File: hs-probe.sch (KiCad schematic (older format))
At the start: 57 parts, among them J1 USB_C_Receptacle_USB2.0, J2 Castellated Vias, J3 Castellated Vias, J4 Castellated Vias, J5 tag-connect-swd, Q101 DMP2110UW-7, U1 hs-probe-stm32, U2 12 MHz, U3 MIC5353, U4 NUF8401MNT4G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

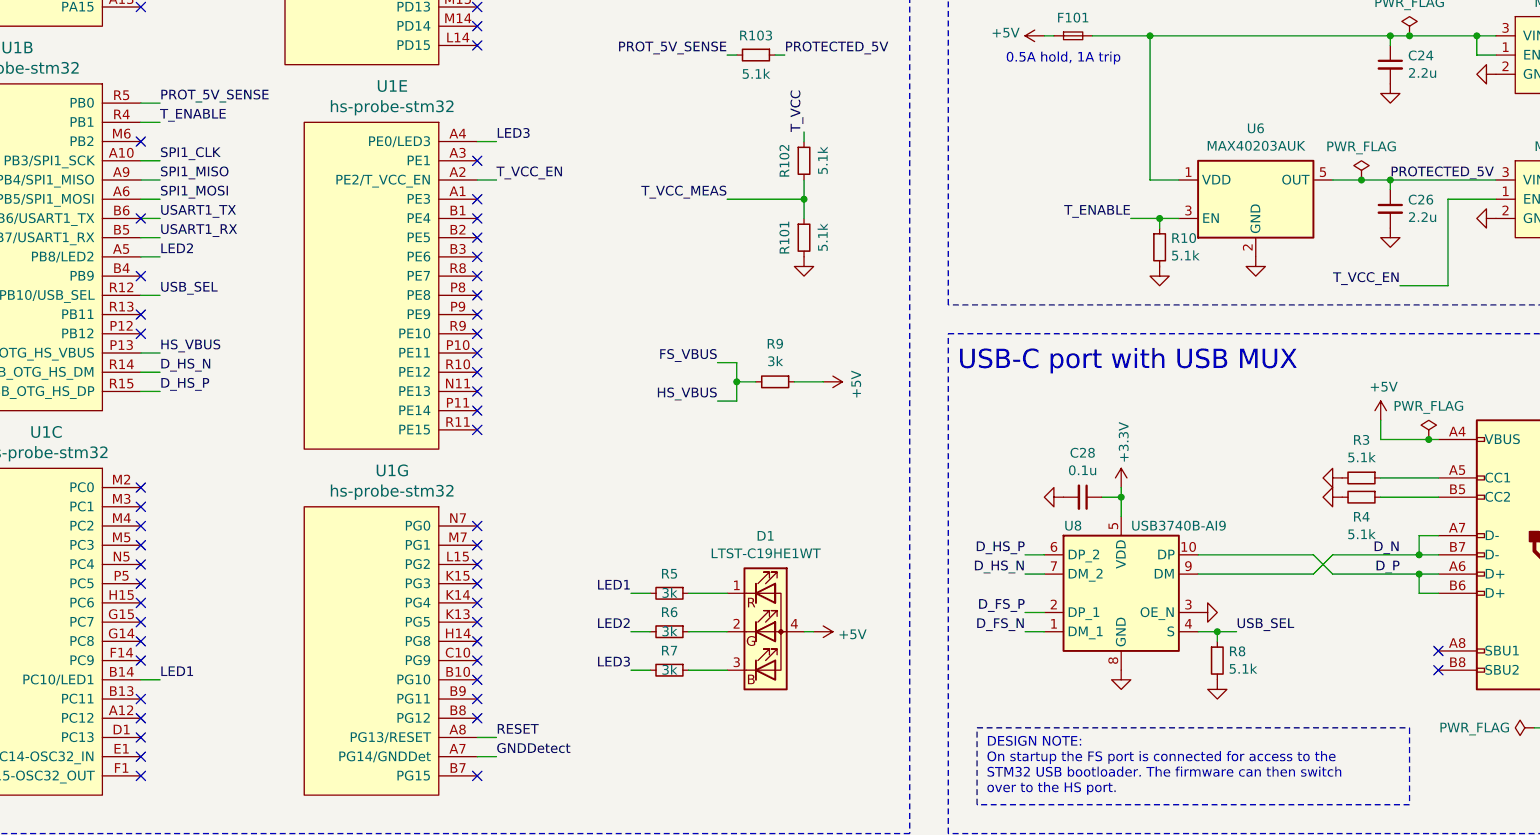
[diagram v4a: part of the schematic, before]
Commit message: v1.4, now without the USB mux
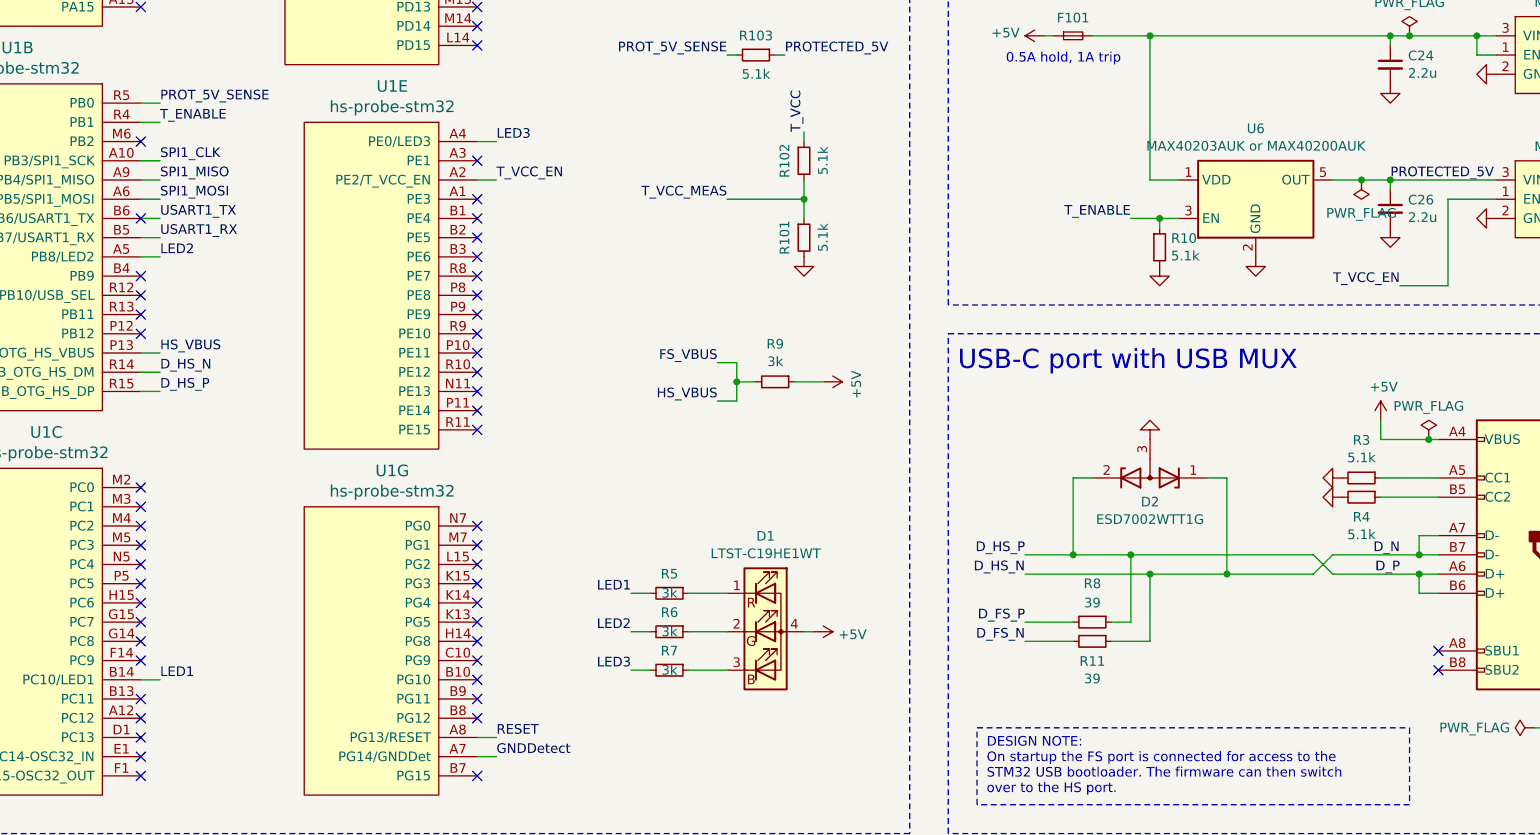
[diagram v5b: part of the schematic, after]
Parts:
- removed C28: 0.1u, passive:C_0402, symbol Device:C_Small
- removed U8: USB3740B-AI9, Package_DFN_QFN:UQFN-10_1.6x2.1mm_P0.5mm, symbol Interface_USB:USB3740B-AI9
- added D2: ESD7002WTT1G, sot:SOT-323, symbol Device:D_Zener_x2_ACom_KKA
- added R11: 39, passive:R_0402, symbol Device:R_Small
- R8: value 5.1k -> 39
- U6: value MAX40203AUK -> MAX40203AUK or MAX40200AUK
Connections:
- net D_N is gone; now on net D_HS_N: J1.A7 (D-), J1.B7 (D-)
- net D_P is gone; now on net D_HS_P: J1.A6 (D+), J1.B6 (D+)
- net D_FS_N: now also R11.2
- net D_FS_P: now also R8.2
- net D_HS_N: now also D2.1 (K), R11.1
- net D_HS_P: now also R8.1, D2.2 (K)
- net GND: now also D2.3 (A); no longer R8.2
- net USB_SEL: no longer names the net of U1.R12 (PB10/USB_SEL)
- net USB_SEL: no longer R8.1
- no-connect marks 84 -> 85
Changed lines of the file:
@@
 Sheet 1 1
 Title "Rusty High-Speed Probe"
-Date "2020-11-28"
-Rev "v1.3"
+Date "2021-05-21"
+Rev "v1.4"
 Comp ""
 Comment1 ""
@@
 	8650 7700 8650 7750
 $Comp
-L Device:C_Small C26
-U 1 1 5E935363
-P 8650 7850
-F 0 "C26" H 8742 7896 50  0000 L CNN
-F 1 "2.2u" H 8742 7805 50  0000 L CNN
-F 2 "passive:C_0402" H 8650 7850 50  0001 C CNN
-F 3 "~" H 8650 7850 50  0001 C CNN
-F 4 "10V, X5R" H 8650 7850 50  0001 C CNN "Tolerance"
-	1    8650 7850
-	1    0    0    -1
-$EndComp
-$Comp
 L Device:C_Small C24
 U 1 1 5E9D42F6
@@
 Text Label 6750 9650 2    50   ~ 0
 D_HS_P
-Wire Wire Line
-	6750 9650 6850 9650
-Wire Wire Line
-	6850 9750 6750 9750
-Text Label 6750 10050 2    50   ~ 0
+Text Label 6750 10100 2    50   ~ 0
 D_FS_N
-Text Label 6750 9950 2    50   ~ 0
+Text Label 6750 10000 2    50   ~ 0
 D_FS_P
-Wire Wire Line
-	6750 9950 6850 9950
-Wire Wire Line
-	6850 10050 6750 10050
-$Comp
-L power:GND #PWR0106
-U 1 1 5F27548A
-P 7250 10250
-F 0 "#PWR0106" H 7250 10000 50  0001 C CNN
-F 1 "GND" H 7255 10077 50  0001 C CNN
-F 2 "" H 7250 10250 50  0001 C CNN
-F 3 "" H 7250 10250 50  0001 C CNN
-	1    7250 10250
-	1    0    0    -1
-$EndComp
-$Comp
-L Device:C_Small C28
-U 1 1 5F275754
-P 7050 9350
-F 0 "C28" V 6821 9350 50  0000 C CNN
-F 1 "0.1u" V 6912 9350 50  0000 C CNN
-F 2 "passive:C_0402" H 7050 9350 50  0001 C CNN
-F 3 "~" H 7050 9350 50  0001 C CNN
-F 4 "25V, X7R" H 7050 9350 50  0001 C CNN "Tolerance"
-	1    7050 9350
-	0    1    1    0
-$EndComp
-$Comp
-L power:+3.3V #PWR0107
-U 1 1 5F276119
-P 7250 9300
-F 0 "#PWR0107" H 7250 9150 50  0001 C CNN
-F 1 "+3.3V" V 7265 9428 50  0000 L CNN
-F 2 "" H 7250 9300 50  0001 C CNN
-F 3 "" H 7250 9300 50  0001 C CNN
-	1    7250 9300
-	1    0    0    -1
-$EndComp
-Wire Wire Line
-	7150 9350 7250 9350
-Wire Wire Line
-	7250 9350 7250 9300
-Wire Wire Line
-	7250 9350 7250 9450
-Connection ~ 7250 9350
-$Comp
-L power:GND #PWR0108
-U 1 1 5F29B742
-P 6950 9350
-F 0 "#PWR0108" H 6950 9100 50  0001 C CNN
-F 1 "GND" H 6955 9177 50  0001 C CNN
-F 2 "" H 6950 9350 50  0001 C CNN
-F 3 "" H 6950 9350 50  0001 C CNN
-	1    6950 9350
-	0    1    1    0
-$EndComp
-$Comp
-L power:GND #PWR0109
-U 1 1 5F2BF882
-P 7650 9950
-F 0 "#PWR0109" H 7650 9700 50  0001 C CNN
-F 1 "GND" H 7655 9777 50  0001 C CNN
-F 2 "" H 7650 9950 50  0001 C CNN
-F 3 "" H 7650 9950 50  0001 C CNN
-	1    7650 9950
-	0    -1   -1   0
-$EndComp
-Wire Wire Line
-	7650 10050 7750 10050
-Text Label 7850 10050 0    50   ~ 0
-USB_SEL
-$Comp
-L Device:R_Small R8
-U 1 1 5F2D2B4D
-P 7750 10200
-F 0 "R8" H 7809 10246 50  0000 L CNN
-F 1 "5.1k" H 7809 10155 50  0000 L CNN
-F 2 "passive:R_0402" H 7750 10200 50  0001 C CNN
-F 3 "~" H 7750 10200 50  0001 C CNN
-F 4 "1%" H 7750 10200 50  0001 C CNN "Tolerance"
-	1    7750 10200
-	1    0    0    -1
-$EndComp
-$Comp
-L power:GND #PWR0110
-U 1 1 5F2D2B53
-P 7750 10300
-F 0 "#PWR0110" H 7750 10050 50  0001 C CNN
-F 1 "GND" H 7755 10127 50  0001 C CNN
-F 2 "" H 7750 10300 50  0001 C CNN
-F 3 "" H 7750 10300 50  0001 C CNN
-	1    7750 10300
-	1    0    0    -1
-$EndComp
-Wire Wire Line
-	7750 10100 7750 10050
-Connection ~ 7750 10050
-Wire Wire Line
-	7750 10050 7850 10050
-$Comp
-L Interface_USB:USB3740B-AI9 U8
-U 1 1 5F2F9B6C
-P 7250 9850
-F 0 "U8" H 7500 10200 50  0000 C CNN
-F 1 "USB3740B-AI9" H 6950 10200 50  0000 C CNN
-F 2 "Package_DFN_QFN:UQFN-10_1.6x2.1mm_P0.5mm" H 8450 9500 50  0001 C CNN
-F 3 "http://ww1.microchip.com/downloads/en/DeviceDoc/00001725D.pdf" H 7250 9750 50  0001 C CNN
-F 4 "USB3740B-AI9-TR" H 7250 9850 50  0001 C CNN "MPN"
-	1    7250 9850
-	-1   0    0    -1
-$EndComp
 $Comp
 L Connector:Conn_01x09_Female J2
@@
 	8350 9750 8800 9750
 Wire Wire Line
-	7650 9650 8250 9650
-Wire Wire Line
 	8350 9650 8250 9750
-Wire Wire Line
-	7650 9750 8250 9750
 Wire Wire Line
 	8350 9650 8800 9650
@@
 Wire Wire Line
 	2250 8100 2150 8100
-Wire Wire Line
-	2250 8300 2150 8300
-Text Label 2250 8300 0    50   ~ 0
-USB_SEL
 Text Label 2250 6700 0    50   ~ 0
 D_FS_P
@@
 P 7950 7800
 F 0 "U6" H 7950 8167 50  0000 C CNN
-F 1 "MAX40203AUK" H 7950 8076 50  0000 C CNN
+F 1 "MAX40203AUK or MAX40200AUK" H 7950 8076 50  0000 C CNN
 F 2 "sot:SOT-23-5" H 7950 8300 50  0001 C CNN
 F 3 "https://datasheets.maximintegrated.com/en/ds/MAX40203.pdf" H 7950 8300 50  0001 C CNN
@@
 F 3 "~" H 8500 7700 50  0001 C CNN
 	1    8500 7700
-	1    0    0    -1
+	-1   0    0    1
 $EndComp
 Connection ~ 8500 7700
@@
 Text Notes 6650 7100 0    50   ~ 0
 0.5A hold, 1A trip
+$Comp
+L Device:C_Small C26
+U 1 1 5E935363
+P 8650 7850
+F 0 "C26" H 8742 7896 50  0000 L CNN
+F 1 "2.2u" H 8742 7805 50  0000 L CNN
+F 2 "passive:C_0402" H 8650 7850 50  0001 C CNN
+F 3 "~" H 8650 7850 50  0001 C CNN
+F 4 "10V, X5R" H 8650 7850 50  0001 C CNN "Tolerance"
+	1    8650 7850
+	1    0    0    -1
+$EndComp
+Wire Wire Line
+	6750 9650 7000 9650
+Wire Wire Line
+	6750 9750 7400 9750
+$Comp
+L Device:R_Small R11
+U 1 1 60B173EB
+P 7100 10100
+F 0 "R11" V 7204 10100 50  0000 C CNN
+F 1 "39" V 7295 10100 50  0000 C CNN
+F 2 "passive:R_0402" H 7100 10100 50  0001 C CNN
+F 3 "~" H 7100 10100 50  0001 C CNN
+F 4 "1%" H 7100 10100 50  0001 C CNN "Tolerance"
+	1    7100 10100
+	0    1    1    0
+$EndComp
+$Comp
+L Device:R_Small R8
+U 1 1 60B17924
+P 7100 10000
+F 0 "R8" V 6900 10000 50  0000 C CNN
+F 1 "39" V 7000 10000 50  0000 C CNN
+F 2 "passive:R_0402" H 7100 10000 50  0001 C CNN
+F 3 "~" H 7100 10000 50  0001 C CNN
+F 4 "1%" H 7100 10000 50  0001 C CNN "Tolerance"
+	1    7100 10000
+	0    1    1    0
+$EndComp
+Wire Wire Line
+	6750 10000 7000 10000
+Wire Wire Line
+	6750 10100 7000 10100
+Wire Wire Line
+	7200 10000 7300 10000
+Wire Wire Line
+	7300 10000 7300 9650
+Connection ~ 7300 9650
+Wire Wire Line
+	7300 9650 8250 9650
+Wire Wire Line
+	7200 10100 7400 10100
+Wire Wire Line
+	7400 10100 7400 9750
+Connection ~ 7400 9750
+Wire Wire Line
+	7400 9750 7800 9750
+$Comp
+L Device:D_Zener_x2_ACom_KKA D2
+U 1 1 60B85F80
+P 7400 9250
+F 0 "D2" H 7400 9375 50  0000 C CNN
+F 1 "ESD7002WTT1G" H 7400 9466 50  0000 C CNN
+F 2 "sot:SOT-323" H 7400 9250 50  0001 C CNN
+F 3 "https://www.onsemi.com/pdf/datasheet/esd7002-d.pdf" H 7400 9250 50  0001 C CNN
+F 4 "ESD7002WTT1G" H 7400 9250 50  0001 C CNN "MFPN"
+	1    7400 9250
+	-1   0    0    1
+$EndComp
+$Comp
+L power:GND #PWR030
+U 1 1 60BAD99F
+P 7400 9050
+F 0 "#PWR030" H 7400 8800 50  0001 C CNN
+F 1 "GND" H 7405 8877 50  0001 C CNN
+F 2 "" H 7400 9050 50  0001 C CNN
+F 3 "" H 7400 9050 50  0001 C CNN
+	1    7400 9050
+	-1   0    0    1
+$EndComp
+Wire Wire Line
+	7100 9250 7000 9250
+Wire Wire Line
+	7000 9250 7000 9650
+Connection ~ 7000 9650
+Wire Wire Line
+	7000 9650 7300 9650
+Wire Wire Line
+	7700 9250 7800 9250
+Wire Wire Line
+	7800 9250 7800 9750
+Connection ~ 7800 9750
+Wire Wire Line
+	7800 9750 8250 9750
+NoConn ~ 2150 8300
 $EndSCHEMATC
